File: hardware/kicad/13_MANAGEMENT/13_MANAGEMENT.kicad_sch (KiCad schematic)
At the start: 9 parts

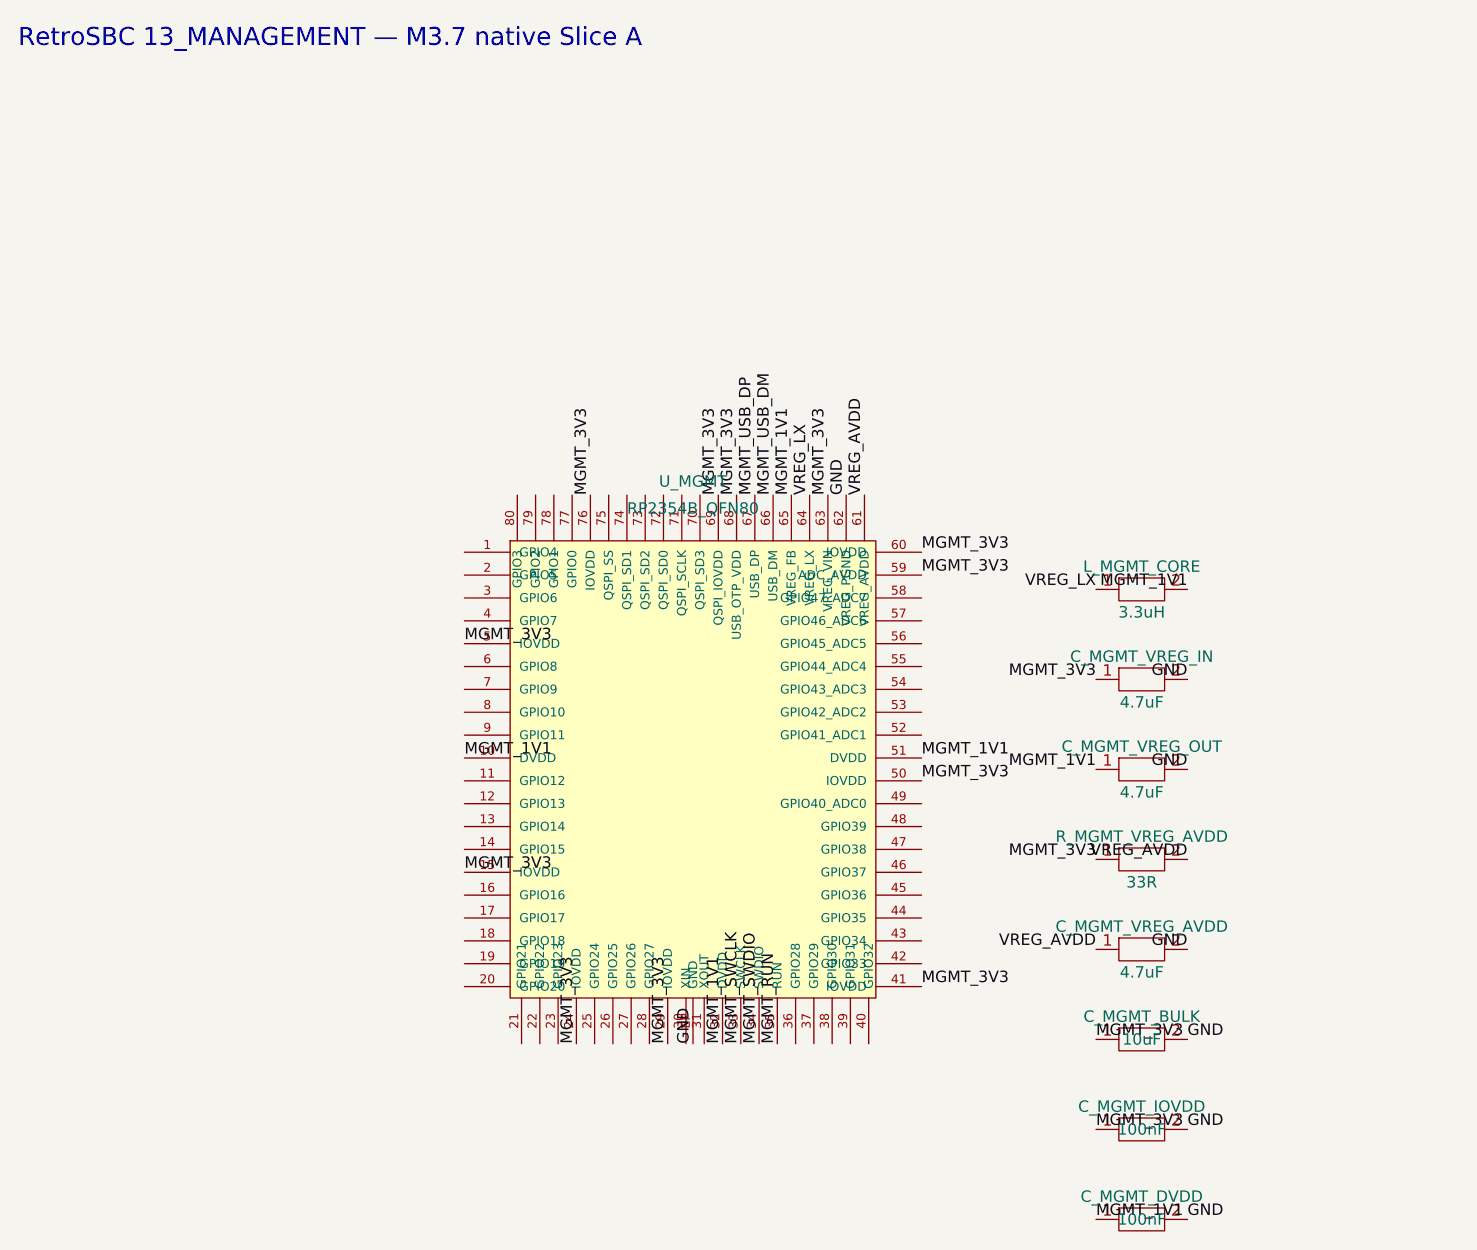
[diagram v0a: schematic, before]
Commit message: M3.7: correct recovery and USB labels to electrical endpoints
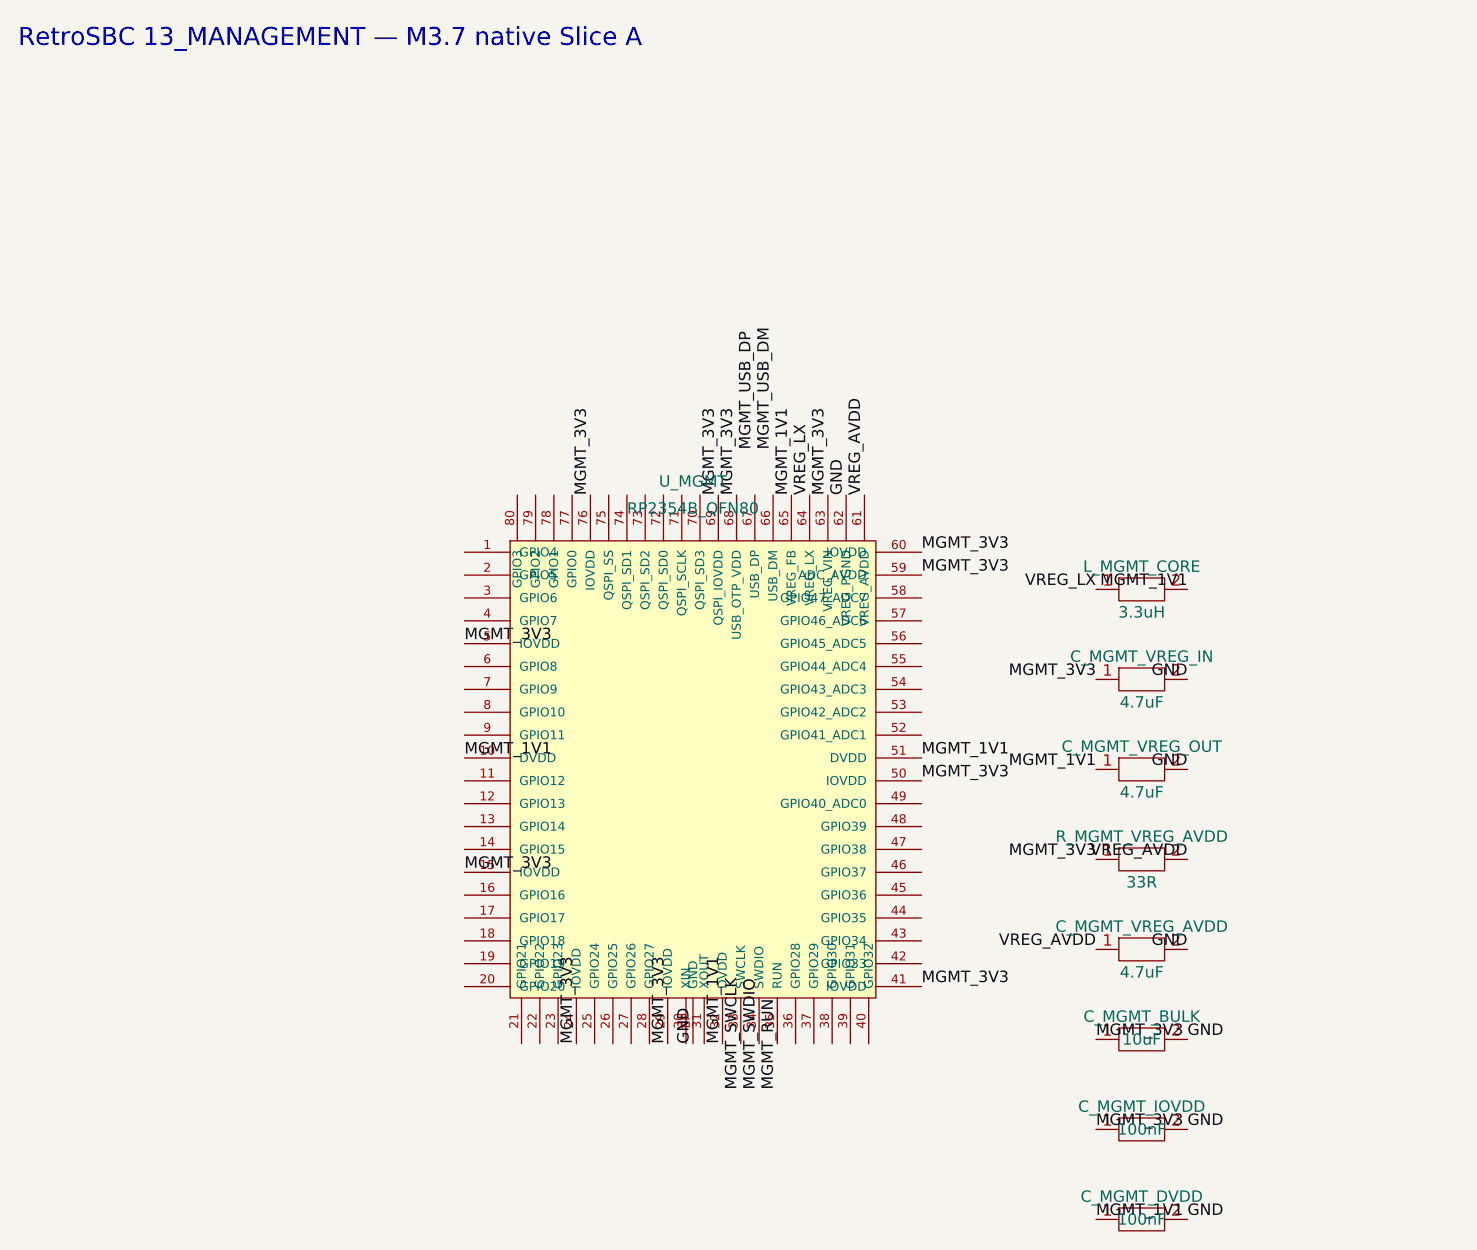
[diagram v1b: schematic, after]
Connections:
- net MGMT_RUN: no longer U_MGMT.35 (RUN)
- net MGMT_SWCLK: no longer U_MGMT.33 (SWCLK)
- net MGMT_SWDIO: no longer U_MGMT.34 (SWDIO)
- net MGMT_USB_DM: no longer U_MGMT.66 (USB_DM)
- net MGMT_USB_DP: no longer U_MGMT.67 (USB_DP)
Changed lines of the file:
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@@
     (effects (font (size 1.27 1.27)) (justify left bottom))
 )
-  (label "MGMT_SWCLK" (at 105.31 130.48 270)
+  (label "MGMT_SWCLK" (at 105.31 135.56 270)
     (effects (font (size 1.27 1.27)) (justify left bottom))
 )
-  (label "MGMT_SWDIO" (at 107.34 130.48 270)
+  (label "MGMT_SWDIO" (at 107.34 135.56 270)
     (effects (font (size 1.27 1.27)) (justify left bottom))
 )
-  (label "MGMT_RUN" (at 109.37 130.48 270)
+  (label "MGMT_RUN" (at 109.37 135.56 270)
     (effects (font (size 1.27 1.27)) (justify left bottom))
 )
-  (label "MGMT_USB_DP" (at 106.87 69.52 90)
+  (label "MGMT_USB_DP" (at 106.87 64.44 90)
     (effects (font (size 1.27 1.27)) (justify left bottom))
 )
-  (label "MGMT_USB_DM" (at 108.90 69.52 90)
+  (label "MGMT_USB_DM" (at 108.90 64.44 90)
     (effects (font (size 1.27 1.27)) (justify left bottom))
 )

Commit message: M3.7: connect recovery and USB labels with explicit native wires
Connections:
- net MGMT_RUN: now also U_MGMT.35 (RUN)
- net MGMT_SWCLK: now also U_MGMT.33 (SWCLK)
- net MGMT_SWDIO: now also U_MGMT.34 (SWDIO)
- net MGMT_USB_DM: now also U_MGMT.66 (USB_DM)
- net MGMT_USB_DP: now also U_MGMT.67 (USB_DP)
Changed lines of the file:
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@@
     (effects (font (size 1.27 1.27)) (justify left bottom))
 )
+  (wire (pts (xy 106.87 69.52) (xy 106.87 64.44)) (stroke (width 0) (type default)))
+  (wire (pts (xy 108.90 69.52) (xy 108.90 64.44)) (stroke (width 0) (type default)))
+  (wire (pts (xy 105.31 130.48) (xy 105.31 135.56)) (stroke (width 0) (type default)))
+  (wire (pts (xy 107.34 130.48) (xy 107.34 135.56)) (stroke (width 0) (type default)))
+  (wire (pts (xy 109.37 130.48) (xy 109.37 135.56)) (stroke (width 0) (type default)))
   (sheet_instances (path "/" (page "1")))
 )

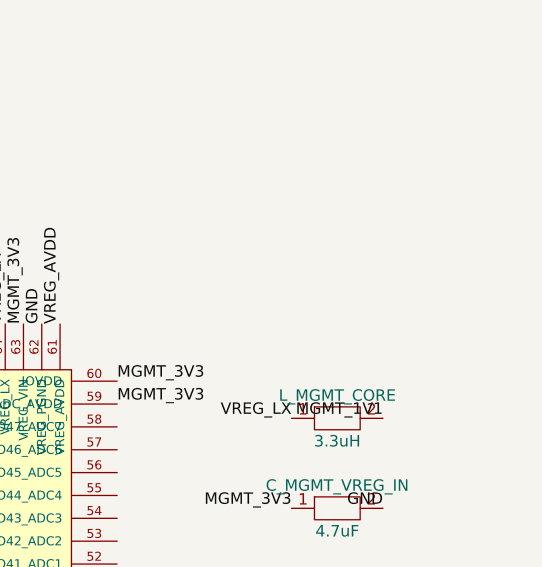
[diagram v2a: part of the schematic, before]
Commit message: M3.7: materialize locked USB 27R series termination
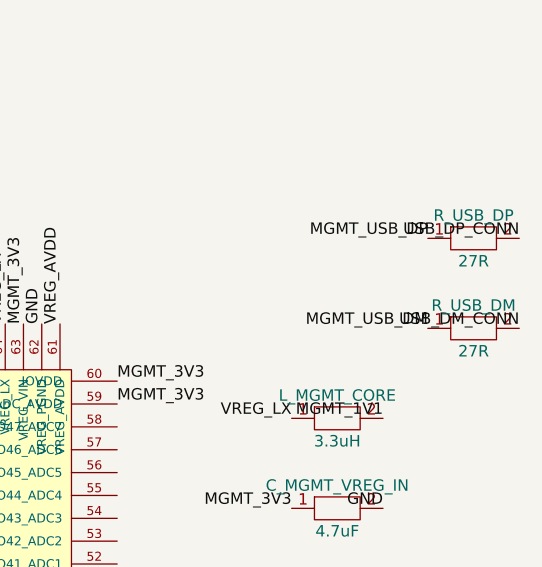
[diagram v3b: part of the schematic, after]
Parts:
- added R_USB_DM, R_USB_DP: 27R, symbol RetroSBC-management:R_LOCAL
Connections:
- net MGMT_USB_DM: now also R_USB_DM.1
- net MGMT_USB_DP: now also R_USB_DP.1
- new net USB_DM_CONN: R_USB_DM.2
- new net USB_DP_CONN: R_USB_DP.2
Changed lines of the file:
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@@
   (wire (pts (xy 107.34 130.48) (xy 107.34 135.56)) (stroke (width 0) (type default)))
   (wire (pts (xy 109.37 130.48) (xy 109.37 135.56)) (stroke (width 0) (type default)))
+  (symbol (lib_id "RetroSBC-management:R_LOCAL") (at 165 60 0) (unit 1)
+    (exclude_from_sim no) (in_bom yes) (on_board yes)
+    (property "Reference" "R_USB_DP" (at 165 57.46 0) (effects (font (size 1.27 1.27))))
+    (property "Value" "27R" (at 165 62.54 0) (effects (font (size 1.27 1.27))))
+    (property "Footprint" "" (at 165 60 0) (effects (font (size 1.27 1.27)) hide))
+    (property "Datasheet" "" (at 165 60 0) (effects (font (size 1.27 1.27)) hide))
+    (property "Description" "RP2354B USB series termination" (at 165 60 0) (effects (font (size 1.27 1.27)) hide))
+    (pin "1")
+    (pin "2")
+    (instances (project "RetroSBC-13-MANAGEMENT" (path "/7a5d3d51-9e2f-4d31-b7cb-9fbd10b8c301/71111111-1111-4111-8111-711111111111" (reference "R_USB_DP") (unit 1))))
+  )
+  (label "MGMT_USB_DP" (at 159.92 60 0) (effects (font (size 1.27 1.27)) (justify right bottom)))
+  (label "USB_DP_CONN" (at 170.08 60 180) (effects (font (size 1.27 1.27)) (justify right bottom)))
+  (symbol (lib_id "RetroSBC-management:R_LOCAL") (at 165 70 0) (unit 1)
+    (exclude_from_sim no) (in_bom yes) (on_board yes)
+    (property "Reference" "R_USB_DM" (at 165 67.46 0) (effects (font (size 1.27 1.27))))
+    (property "Value" "27R" (at 165 72.54 0) (effects (font (size 1.27 1.27))))
+    (property "Footprint" "" (at 165 70 0) (effects (font (size 1.27 1.27)) hide))
+    (property "Datasheet" "" (at 165 70 0) (effects (font (size 1.27 1.27)) hide))
+    (property "Description" "RP2354B USB series termination" (at 165 70 0) (effects (font (size 1.27 1.27)) hide))
+    (pin "1")
+    (pin "2")
+    (instances (project "RetroSBC-13-MANAGEMENT" (path "/7a5d3d51-9e2f-4d31-b7cb-9fbd10b8c301/72111111-1111-4111-8111-722222222222" (reference "R_USB_DM") (unit 1))))
+  )
+  (label "MGMT_USB_DM" (at 159.92 70 0) (effects (font (size 1.27 1.27)) (justify right bottom)))
+  (label "USB_DM_CONN" (at 170.08 70 180) (effects (font (size 1.27 1.27)) (justify right bottom)))
   (sheet_instances (path "/" (page "1")))
 )

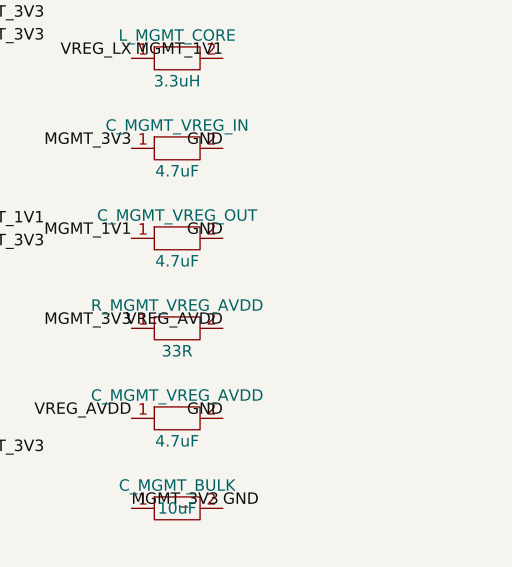
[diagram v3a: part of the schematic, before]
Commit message: M3.7: materialize locked USB-C CC Rd network
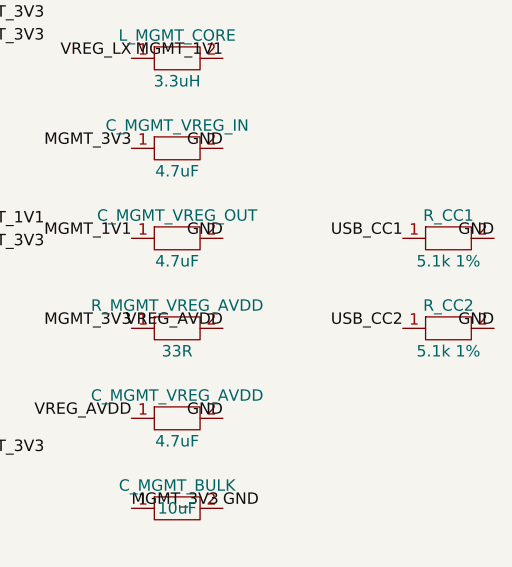
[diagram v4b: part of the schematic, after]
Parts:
- added R_CC1, R_CC2: 5.1k 1%, symbol RetroSBC-management:R_LOCAL
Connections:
- net GND: now also R_CC1.2, R_CC2.2
- new net USB_CC1: R_CC1.1
- new net USB_CC2: R_CC2.1
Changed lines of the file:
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@@
   (label "MGMT_USB_DM" (at 159.92 70 0) (effects (font (size 1.27 1.27)) (justify right bottom)))
   (label "USB_DM_CONN" (at 170.08 70 180) (effects (font (size 1.27 1.27)) (justify right bottom)))
+  (symbol (lib_id "RetroSBC-management:R_LOCAL") (at 180 100 0) (unit 1)
+    (exclude_from_sim no) (in_bom yes) (on_board yes)
+    (property "Reference" "R_CC1" (at 180 97.46 0) (effects (font (size 1.27 1.27))))
+    (property "Value" "5.1k 1%" (at 180 102.54 0) (effects (font (size 1.27 1.27))))
+    (property "Footprint" "" (at 180 100 0) (effects (font (size 1.27 1.27)) hide))
+    (property "Datasheet" "" (at 180 100 0) (effects (font (size 1.27 1.27)) hide))
+    (property "Description" "USB-C UFP CC Rd" (at 180 100 0) (effects (font (size 1.27 1.27)) hide))
+    (pin "1")
+    (pin "2")
+    (instances (project "RetroSBC-13-MANAGEMENT" (path "/7a5d3d51-9e2f-4d31-b7cb-9fbd10b8c301/73111111-1111-4111-8111-733333333333" (reference "R_CC1") (unit 1))))
+  )
+  (label "USB_CC1" (at 174.92 100 0) (effects (font (size 1.27 1.27)) (justify right bottom)))
+  (label "GND" (at 185.08 100 180) (effects (font (size 1.27 1.27)) (justify right bottom)))
+  (symbol (lib_id "RetroSBC-management:R_LOCAL") (at 180 110 0) (unit 1)
+    (exclude_from_sim no) (in_bom yes) (on_board yes)
+    (property "Reference" "R_CC2" (at 180 107.46 0) (effects (font (size 1.27 1.27))))
+    (property "Value" "5.1k 1%" (at 180 112.54 0) (effects (font (size 1.27 1.27))))
+    (property "Footprint" "" (at 180 110 0) (effects (font (size 1.27 1.27)) hide))
+    (property "Datasheet" "" (at 180 110 0) (effects (font (size 1.27 1.27)) hide))
+    (property "Description" "USB-C UFP CC Rd" (at 180 110 0) (effects (font (size 1.27 1.27)) hide))
+    (pin "1")
+    (pin "2")
+    (instances (project "RetroSBC-13-MANAGEMENT" (path "/7a5d3d51-9e2f-4d31-b7cb-9fbd10b8c301/74111111-1111-4111-8111-744444444444" (reference "R_CC2") (unit 1))))
+  )
+  (label "USB_CC2" (at 174.92 110 0) (effects (font (size 1.27 1.27)) (justify right bottom)))
+  (label "GND" (at 185.08 110 180) (effects (font (size 1.27 1.27)) (justify right bottom)))
   (sheet_instances (path "/" (page "1")))
 )
